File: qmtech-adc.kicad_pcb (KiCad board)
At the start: 4 copper layers, 60 x 45 mm, 49 parts

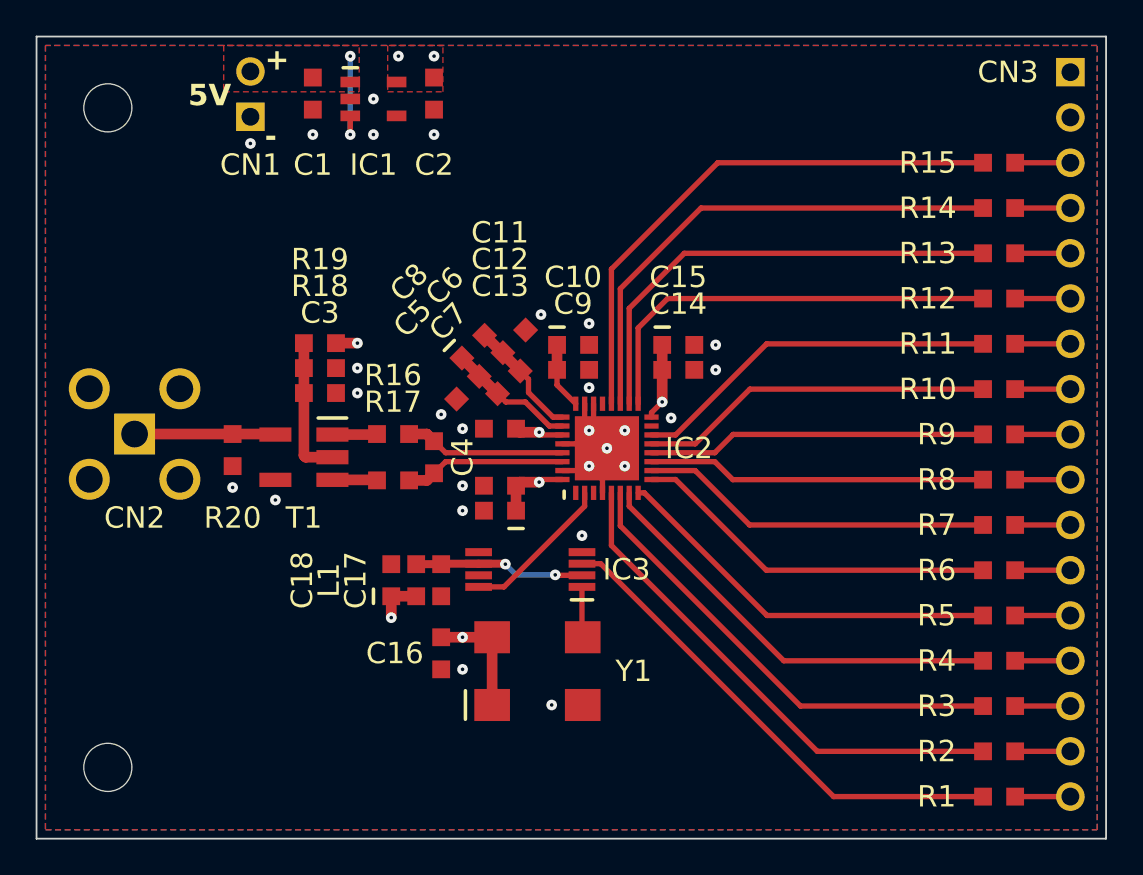
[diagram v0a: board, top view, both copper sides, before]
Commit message: replace C1952781 with C7171
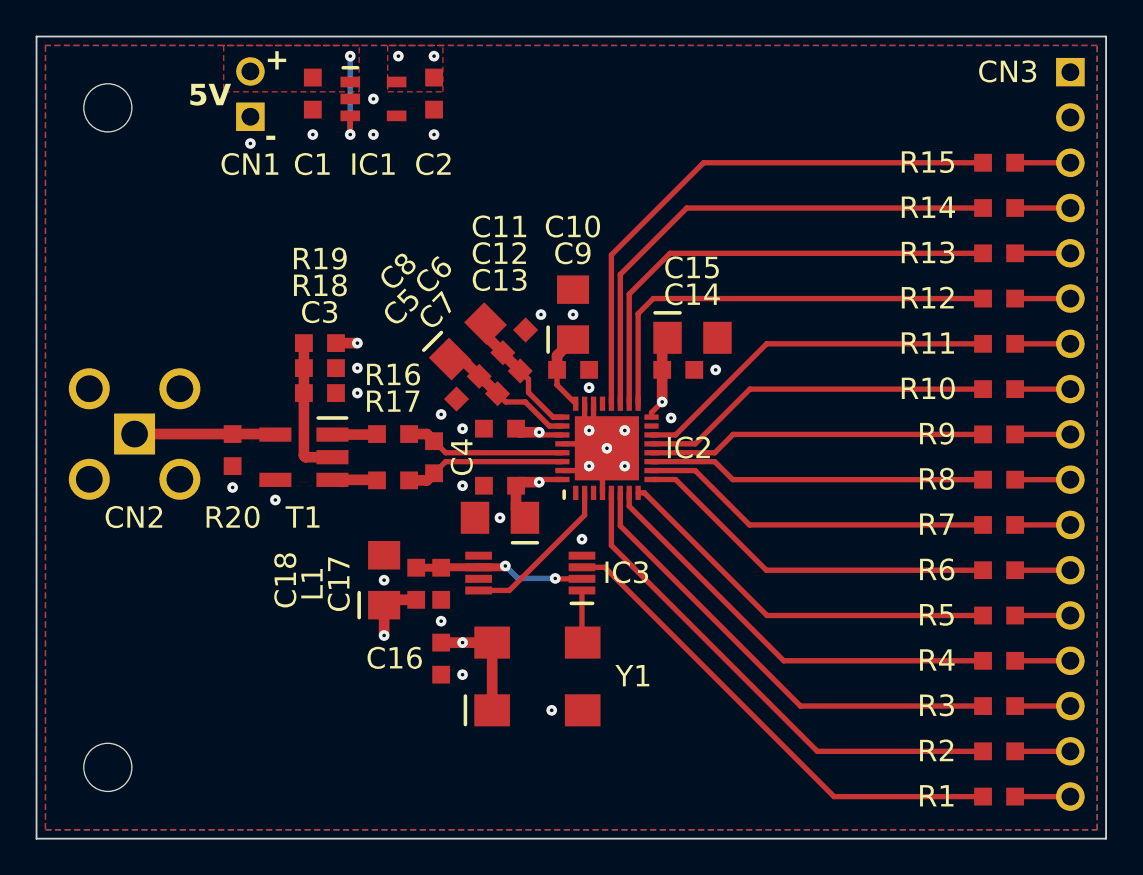
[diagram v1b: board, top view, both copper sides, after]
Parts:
- C10, C13, C15, C18, C8: footprint footprints:0603T -> footprints:CASE-A-3216
- moved C10 1.70 mm to (98.1, 63.6), turned to 90 degrees
- moved C15 0.89 mm to (104.8, 64.9)
- moved C8 0.42 mm to (92.2, 65.1)
- moved C13 0.40 mm to (94.0, 75.0)
- moved C18 0.40 mm to (87.5, 78.5)
- moved C16 0.30 mm to (90.7, 82.9)
- moved Y1 0.30 mm to (96.1, 83.9)
- moved C17 0.20 mm to (90.7, 78.7)
- moved L1 0.20 mm to (89.3, 78.7)
- moved IC3 0.20 mm to (95.7, 78.1)
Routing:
- net AVDD: track 17.3 -> 18.9 mm
- net VREF: track 3.73 -> 4.41 mm
- net REFB: track 6.73 -> 7.33 mm
- net REFT: track 7.25 -> 7.85 mm
- net DVDD: track 4.30 -> 4.82 mm
- net GND: vias 27 -> 28
